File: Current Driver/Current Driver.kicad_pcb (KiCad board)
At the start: 2 copper layers, 45 parts, among them Q1 BC817, Q2 BC807, U1 ADA4622-2xCP, U2 ADA4622-2xCP

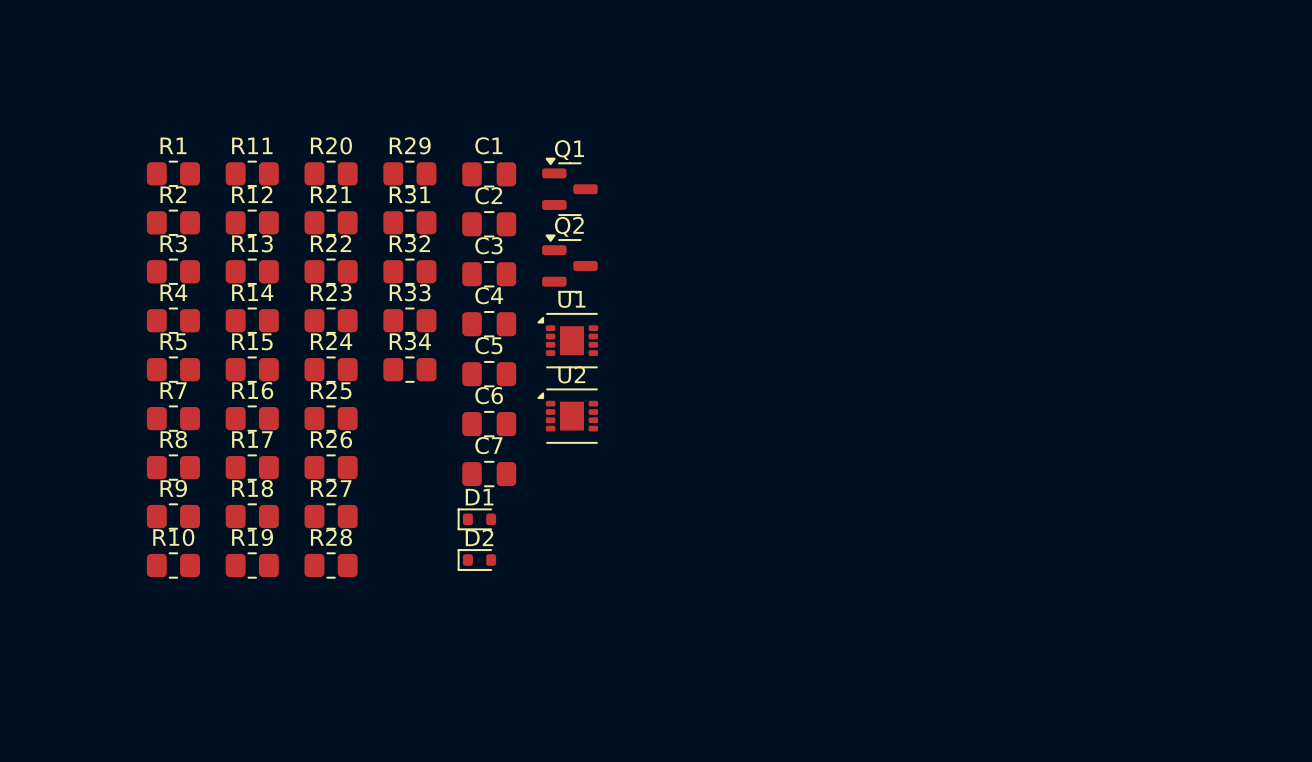
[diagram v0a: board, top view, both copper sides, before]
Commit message: schematic update
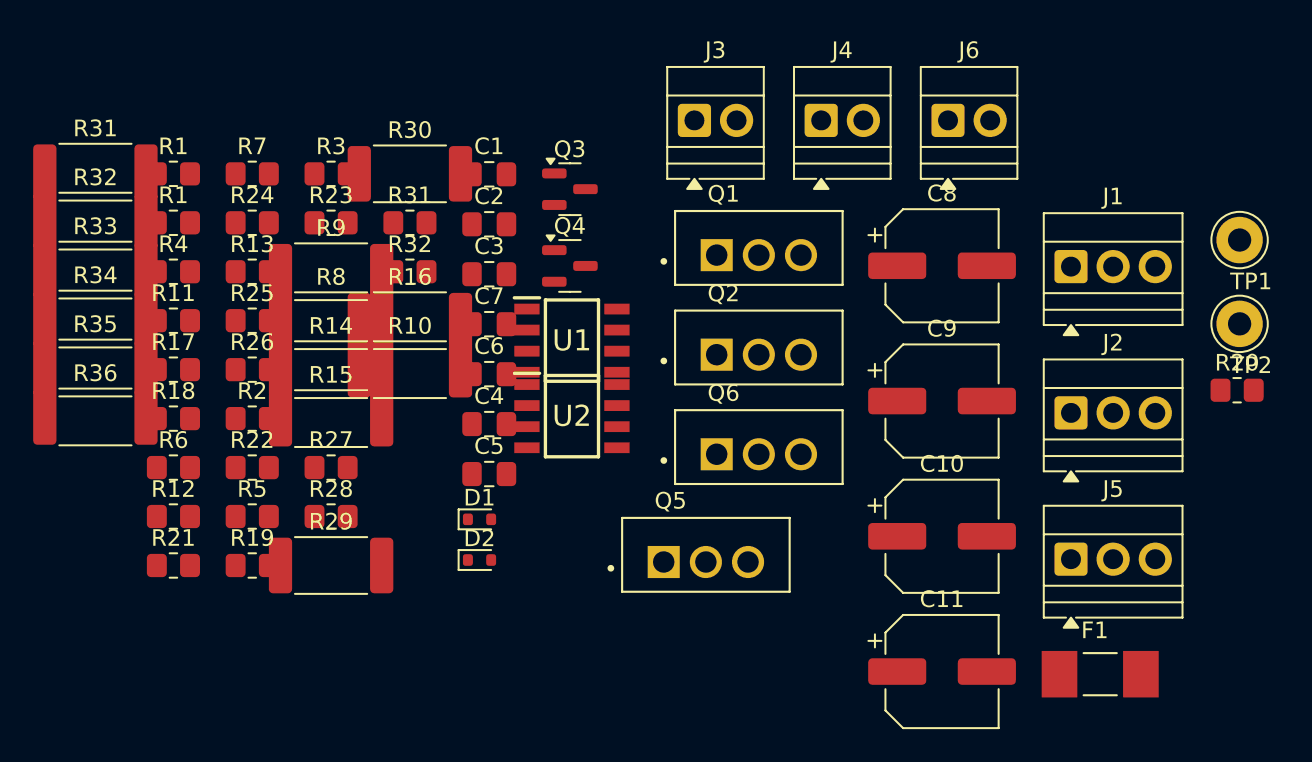
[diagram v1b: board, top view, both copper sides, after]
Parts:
- added C10: 25u, Capacitor_SMD:CP_Elec_6.3x7.7, F.Cu at (82.5, 61.7)
- added C11: 25u, Capacitor_SMD:CP_Elec_6.3x7.7, F.Cu at (82.5, 69.8)
- added C8: 25u, Capacitor_SMD:CP_Elec_6.3x7.7, F.Cu at (82.5, 45.4)
- added C9: 25u, Capacitor_SMD:CP_Elec_6.3x7.7, F.Cu at (82.5, 53.5)
- added F1: Fuse, component_lib:2410 FUSE, F.Cu at (92.0, 70.0)
- added J1: VP BJT Conn, TerminalBlock:TerminalBlock_Xinya_XY308-2.54-3P_1x03_P2.54mm_Horizontal, F.Cu at (90.3, 45.4)
- added J2: VN BJT Conn, TerminalBlock:TerminalBlock_Xinya_XY308-2.54-3P_1x03_P2.54mm_Horizontal, F.Cu at (90.3, 54.3)
- added J3: Load, TerminalBlock:TerminalBlock_Xinya_XY308-2.54-2P_1x02_P2.54mm_Horizontal, F.Cu at (67.6, 36.6)
- added J4: Input, TerminalBlock:TerminalBlock_Xinya_XY308-2.54-2P_1x02_P2.54mm_Horizontal, F.Cu at (75.2, 36.6)
- added J5: PWR In, TerminalBlock:TerminalBlock_Xinya_XY308-2.54-3P_1x03_P2.54mm_Horizontal, F.Cu at (90.3, 63.1)
- added J6: Add. R, TerminalBlock:TerminalBlock_Xinya_XY308-2.54-2P_1x02_P2.54mm_Horizontal, F.Cu at (82.9, 36.6)
- added Q1: D45H11, component_lib:D44H11G, F.Cu at (71.5, 44.7)
- added Q2: D45H11G, component_lib:D44H11G, F.Cu at (71.5, 50.7)
- added Q5: D44H11G, component_lib:D44H11G, F.Cu at (68.3, 63.2)
- added Q6: D44H11G, component_lib:D44H11G, F.Cu at (71.5, 56.7)
- added R20: 10kΩ, Resistor_SMD:R_0805_2012Metric_Pad1.20x1.40mm_HandSolder, F.Cu at (100.3, 52.9)
- added R31: R, Resistor_SMD:R_2512_6332Metric_Pad1.40x3.35mm_HandSolder, F.Cu at (31.5, 39.8)
- added R32: R, Resistor_SMD:R_2512_6332Metric_Pad1.40x3.35mm_HandSolder, F.Cu at (31.5, 42.7)
- added R33: 200m, Resistor_SMD:R_2512_6332Metric_Pad1.40x3.35mm_HandSolder, F.Cu at (31.5, 45.6)
- added R34: 200m, Resistor_SMD:R_2512_6332Metric_Pad1.40x3.35mm_HandSolder, F.Cu at (31.5, 48.6)
- added R35: 200m, Resistor_SMD:R_2512_6332Metric_Pad1.40x3.35mm_HandSolder, F.Cu at (31.5, 51.5)
- added R36: 200m, Resistor_SMD:R_2512_6332Metric_Pad1.40x3.35mm_HandSolder, F.Cu at (31.5, 54.5)
- added TP1: V_REF, TestPoint:TestPoint_Loop_D2.60mm_Drill1.4mm_Beaded, F.Cu at (100.4, 43.8)
- added TP2: DRV_IN, TestPoint:TestPoint_Loop_D2.60mm_Drill1.4mm_Beaded, F.Cu at (100.4, 48.9)
- R1: renamed from R2; value 300Ω -> 1kΩ
- R10: renamed from R34; footprint Resistor_SMD:R_0805_2012Metric_Pad1.20x1.40mm_HandSolder -> Resistor_SMD:R_2512_6332Metric_Pad1.40x3.35mm_HandSolder
- R14: renamed from R24; value 430m -> 200m; footprint Resistor_SMD:R_0805_2012Metric_Pad1.20x1.40mm_HandSolder -> Resistor_SMD:R_2512_6332Metric_Pad1.40x3.35mm_HandSolder
- R15: renamed from R25; value 430m -> 200m; footprint Resistor_SMD:R_0805_2012Metric_Pad1.20x1.40mm_HandSolder -> Resistor_SMD:R_2512_6332Metric_Pad1.40x3.35mm_HandSolder
- R16: renamed from R33; footprint Resistor_SMD:R_0805_2012Metric_Pad1.20x1.40mm_HandSolder -> Resistor_SMD:R_2512_6332Metric_Pad1.40x3.35mm_HandSolder
- R29: renamed from R28; value 430mΩ -> 200m; footprint Resistor_SMD:R_0805_2012Metric_Pad1.20x1.40mm_HandSolder -> Resistor_SMD:R_2512_6332Metric_Pad1.40x3.35mm_HandSolder
- R30: renamed from R29; value 430mΩ -> 200m; footprint Resistor_SMD:R_0805_2012Metric_Pad1.20x1.40mm_HandSolder -> Resistor_SMD:R_2512_6332Metric_Pad1.40x3.35mm_HandSolder
- R8: renamed from R23; value 430m -> 200m; footprint Resistor_SMD:R_0805_2012Metric_Pad1.20x1.40mm_HandSolder -> Resistor_SMD:R_2512_6332Metric_Pad1.40x3.35mm_HandSolder
- R9: renamed from R22; value 430m -> 200m; footprint Resistor_SMD:R_0805_2012Metric_Pad1.20x1.40mm_HandSolder -> Resistor_SMD:R_2512_6332Metric_Pad1.40x3.35mm_HandSolder
- U1, U2: footprint Package_CSP:LFCSP-8-1EP_3x3mm_P0.5mm_EP1.45x1.74mm -> component_lib:ADA4522
- renumbered C6 to C4, C7 to C5, C5 to C6, C4 to C7, Q1 to Q3, Q2 to Q4, R4 to R11, R9 to R12, R5 to R17, R7 to R18, R16 to R2, R10 to R21, R17 to R22, R21 to R23, R12 to R24, R14 to R25, R15 to R26, R26 to R27, R27 to R28, R20 to R3, R3 to R4, R18 to R5, R8 to R6, R11 to R7
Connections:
- net /VNEG_DRIV renamed /VNEG_B
- net /VPOS_DRIV renamed /VPOS_B
- Q3 pad 2: Net-(Q1-E) -> Net-(Q2-C)
- Q4 pad 2: Net-(Q2-E) -> Net-(Q4-E)
- R1 pad 1: Net-(R2-Pad1) -> +3.3V
- R1 pad 2: /V_REF -> Net-(U2B--)
- R14 pad 2: Net-(Q2-E) -> Net-(R14-Pad2)
- R4 pad 1: /V_REF -> Net-(U2B--)
- R8 pad 1: Net-(Q1-E) -> Net-(R34-Pad2)
- U2 pad 5: (no net) -> /V_REF
- U2 pad 6: (no net) -> Net-(U2B--)
- U2 pad 7: (no net) -> /V_REF

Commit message: Minor Edit PCB
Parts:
- removed the R1 at (36.2, 42.8)
- removed the R1 at (36.2, 39.9)
- removed R27, R28: 430mΩ, Resistor_SMD:R_0805_2012Metric_Pad1.20x1.40mm_HandSolder
- removed the R31 at (50.5, 42.8)
- removed the R31 at (31.5, 39.8)
- removed the R32 at (31.5, 42.7)
- removed the R32 at (50.5, 45.8)
- added R1: 1kΩ, Resistor_SMD:R_0805_2012Metric_Pad1.20x1.40mm_HandSolder, F.Cu at (51.8, 61.0)
- added R31: R, Resistor_SMD:R_2512_6332Metric_Pad1.40x3.35mm_HandSolder, F.Cu at (34.4, 31.7)
- added R32: R, Resistor_SMD:R_2512_6332Metric_Pad1.40x3.35mm_HandSolder, F.Cu at (34.4, 36.6)
- moved TP2 70.7 mm to (31.9, 66.2)
- moved TP1 70.7 mm to (31.9, 61.2)
- moved R20 42.5 mm to (61.3, 69.9)
- moved C10 41.9 mm to (44.2, 44.7)
- moved C11 41.9 mm to (44.2, 52.8)
- moved C8 41.9 mm to (44.2, 28.4)
- moved C9 41.9 mm to (44.2, 36.5)
- moved J1 41.9 mm to (52.0, 28.4)
- moved J2 41.9 mm to (52.0, 37.2)
- moved J5 41.9 mm to (52.0, 46.1)
- moved Q3 41.5 mm to (31.8, 71.2)
- moved Q4 41.5 mm to (31.8, 75.8)
- moved F1 38.9 mm to (53.7, 76.5)
- moved U2 37.8 mm to (25.1, 68.5)
- moved U1 37.1 mm to (25.1, 61.9)
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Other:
- board outline added: 60 x 60 mm

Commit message: Update Current Driver.kicad_pcb
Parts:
- J4: footprint TerminalBlock:TerminalBlock_Xinya_XY308-2.54-2P_1x02_P2.54mm_Horizontal -> TerminalBlock:TerminalBlock_Xinya_XY308-2.54-3P_1x03_P2.54mm_Horizontal
- moved R32 101.9 mm to (103.5, 111.4), turned to -90 degrees
- moved C8 97.8 mm to (70.7, 122.5)
- moved C9 97.6 mm to (89.0, 123.2)
- moved J2 96.4 mm to (96.3, 122.8)
- moved R16 94.3 mm to (98.0, 111.5), turned to 90 degrees
- moved R15 92.4 mm to (89.1, 113.3), turned to 180 degrees
- moved R30 91.7 mm to (63.0, 113.9), turned to 180 degrees
- moved R14 90.9 mm to (88.9, 106.5), turned to 180 degrees
- moved R8 87.4 mm to (88.5, 87.2)
- moved R10 85.8 mm to (98.0, 82.3), turned to -90 degrees
- moved R31 85.3 mm to (103.0, 82.3), turned to -90 degrees
- moved R36 81.9 mm to (89.0, 117.2)
- moved R9 80.2 mm to (88.4, 81.2)
- moved Q6 75.9 mm to (78.8, 120.6), turned to -90 degrees
- moved R35 74.7 mm to (88.9, 102.5)
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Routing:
- net /uC_SIGNAL: track 0.00 -> 51.5 mm
- net +3.3V: track 0.00 -> 28.4 mm
- net /CURRENT_FEEDBACK: track 0.00 -> 28.2 mm
- net Net-(U2A--): track 0.00 -> 18.9 mm
- net Net-(C3-Pad1): track 0.00 -> 16.4 mm
- net /V_REF: track 0.00 -> 15.0 mm
- net /DRIVING_INPUT: track 0.00 -> 11.3 mm
- net Net-(C1-Pad2): track 0.00 -> 10.7 mm
- net Net-(C2-Pad2): track 0.00 -> 10.2 mm
- net Net-(U1A--): track 0.00 -> 9.52 mm
- net Net-(U1B--): track 0.00 -> 7.09 mm
- net /SIGNAL_INPUT: track 0.00 -> 5.73 mm
- net -VCC: track 0.00 -> 5.23 mm
- net Net-(D1-A): track 0.00 -> 4.75 mm
- net Net-(U1A-+): track 0.00 -> 4.64 mm
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
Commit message: PCB_wersja1
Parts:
- moved C11 51.6 mm to (60.7, 115.1)
- moved C10 37.4 mm to (60.7, 107.3)
- moved C9 23.7 mm to (65.2, 123.2), turned to 180 degrees
- moved C8 15.6 mm to (55.1, 123.4), turned to 180 degrees
- moved R30 10.6 mm to (73.6, 114.0), turned to 90 degrees
- moved R29 7.80 mm to (68.0, 114.0), turned to -90 degrees
- moved R22 2.40 mm to (70.8, 104.2)
- moved R23 1.77 mm to (75.1, 106.6)
- moved R19 1.72 mm to (70.8, 102.2)
- moved J2 1.70 mm to (96.3, 121.2)
- moved R36 1.54 mm to (88.8, 115.7)
- moved R15 1.54 mm to (88.9, 111.7)
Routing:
- net -VCC: track 5.23 -> 161.0 mm, vias 0 -> 3
- net +VCC: track 4.19 -> 143.6 mm, vias 0 -> 4
- net /CURRENT_FEEDBACK: track 28.2 -> 101.8 mm, vias 0 -> 4
- net /VPOS_B: track 0.00 -> 61.5 mm, vias 0 -> 3
- net /DRIVING_OUTPUT: track 0.00 -> 53.1 mm, vias 0 -> 2
- net /VNEG_B: track 0.00 -> 50.3 mm, vias 0 -> 3
- net Net-(Q4-E): track 0.00 -> 27.3 mm
- net Net-(Q6-C): track 0.00 -> 18.0 mm, vias 0 -> 2
- net Net-(Q2-C): track 0.00 -> 16.8 mm
- net /DRIVER_OUTPUT: track 0.00 -> 12.0 mm
- net /DRIVING_INPUT: track 11.3 -> 21.1 mm
- net /VPOS_C: track 0.00 -> 9.44 mm
- net /VNEG_C: track 0.00 -> 8.64 mm
- net Net-(R10-Pad1): track 0.00 -> 8.17 mm
- net Net-(R34-Pad2): track 0.00 -> 7.95 mm
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- added copper zone on B.Cu, net GND
- added copper zone on F.Cu, net GND

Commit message: PCB_v2
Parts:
- moved R34 4.61 mm to (88.1, 86.7)
- moved R35 4.16 mm to (88.9, 106.6), turned to 180 degrees
- moved R14 3.95 mm to (88.9, 102.5)
- moved R8 3.60 mm to (88.1, 90.7)
- moved D1 3.24 mm to (69.3, 89.9)
- moved J4 1.48 mm to (51.9, 105.5)
- moved C2 1.39 mm to (60.5, 83.3)
- moved R12 1.39 mm to (56.5, 83.3)
- moved R7 1.39 mm to (58.5, 83.3)
- moved R20 1.22 mm to (96.9, 99.1)
- moved R21 0.77 mm to (63.2, 89.2)
- moved C5 0.58 mm to (63.2, 93.3)
- moved R31 0.53 mm to (103.5, 82.3)
- turned C3 to -90 degrees
- turned R16 to -90 degrees
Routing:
- net Net-(C1-Pad2): track 10.7 -> 23.9 mm
- net +VCC: track 143.6 -> 131.9 mm
- net Net-(Q4-E): track 27.3 -> 18.6 mm, vias 0 -> 2
- net /DRIVING_INPUT: track 21.1 -> 26.1 mm, vias 0 -> 3
- net /DRIVING_OUTPUT: track 53.1 -> 48.6 mm, vias 2 -> 0
- net /uC_SIGNAL: track 55.6 -> 51.5 mm, vias 2 -> 0
- net /CURRENT_FEEDBACK: track 101.8 -> 97.7 mm, vias 4 -> 3
- net Net-(R14-Pad2): track 4.00 -> 7.77 mm
- net /VNEG_B: track 50.3 -> 47.1 mm, vias 3 -> 0
- net Net-(R16-Pad2): track 5.57 -> 8.45 mm
- net Net-(Q2-C): track 16.8 -> 19.6 mm, vias 0 -> 2
- net Net-(Q6-C): track 18.0 -> 15.2 mm, vias 2 -> 0
- net -VCC: track 161.0 -> 163.6 mm, vias 3 -> 2
- net GND: track 2.21 -> 0.00 mm, vias 1 -> 0
- net Net-(U1A--): track 9.52 -> 7.63 mm
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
